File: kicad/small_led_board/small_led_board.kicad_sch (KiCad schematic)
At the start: 106 parts, among them J1 Breakout to FPGA, Q1 IRLZ44N, Q10 IRF4905, Q11 IRF4905, Q12 IRF4905, Q13 IRF4905, Q14 IRF4905, Q15 IRLZ44N, Q16 IRLZ44N, Q17 IRLZ44N, Q18 IRLZ44N, Q19 IRLZ44N, Q2 IRLZ44N, Q20 IRLZ44N, Q3 IRLZ44N, Q4 IRLZ44N, Q5 IRLZ44N, Q6 IRLZ44N, Q7 IRLZ44N, Q8 IRLZ44N, Q9 IRF4905, U1 74HC595, U2 74HC595, U3 74HC595

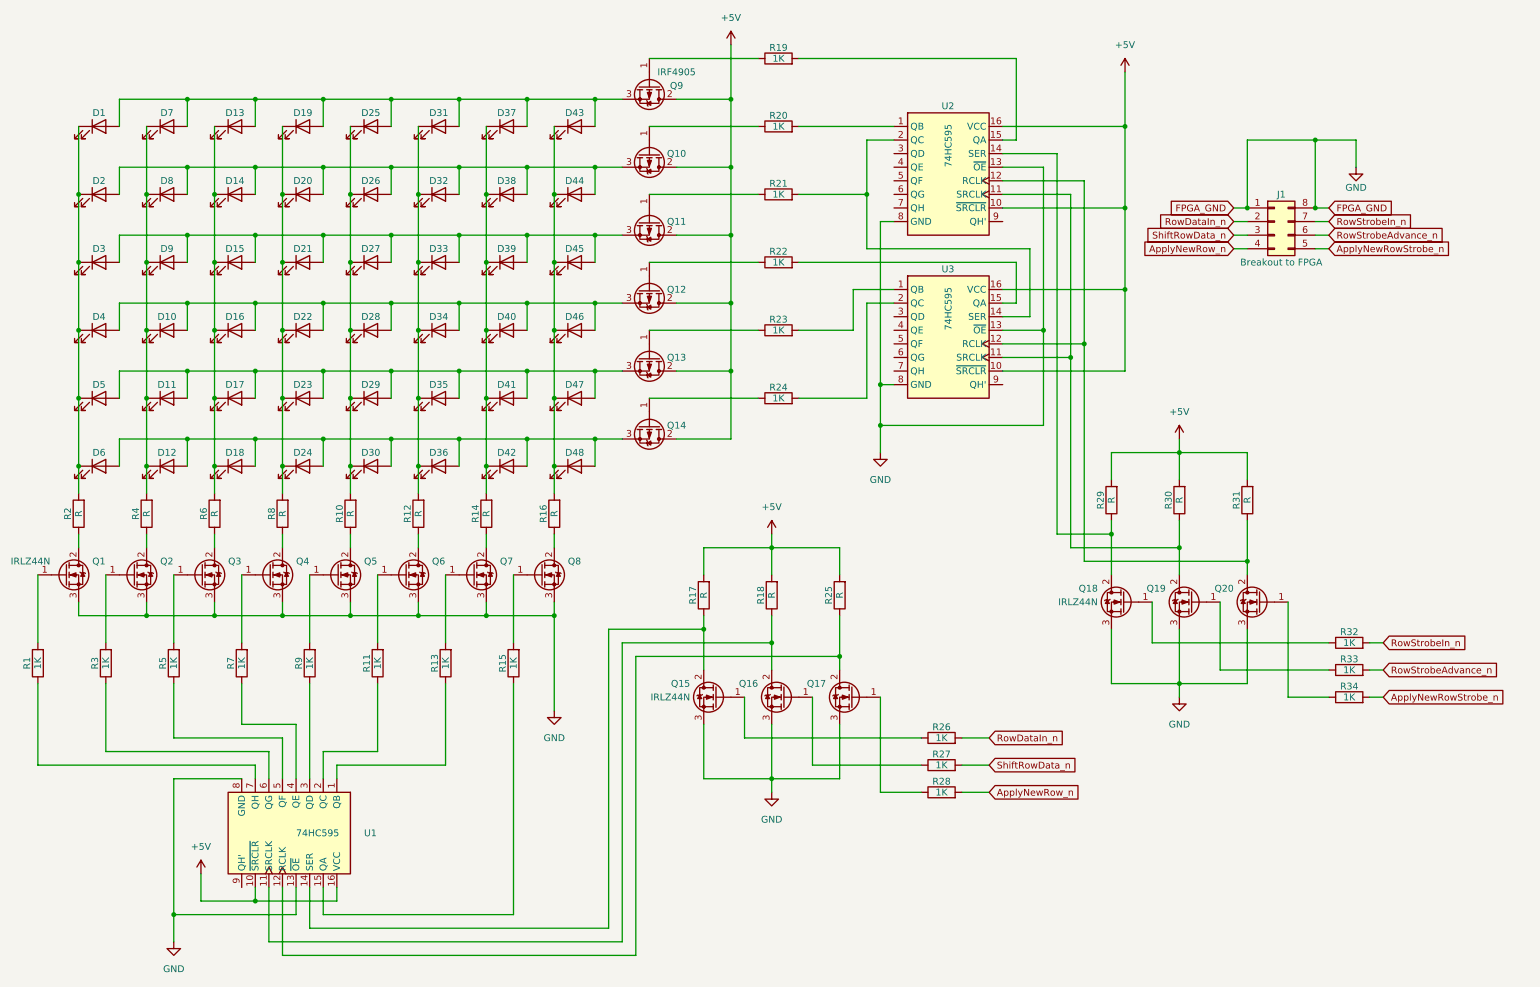
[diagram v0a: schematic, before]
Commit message: small_led_board: Schematic updated, DRC pass
- Schematic passes DRC check without any issue
- LED resistors still need to be calculated after that the schematic should be finished
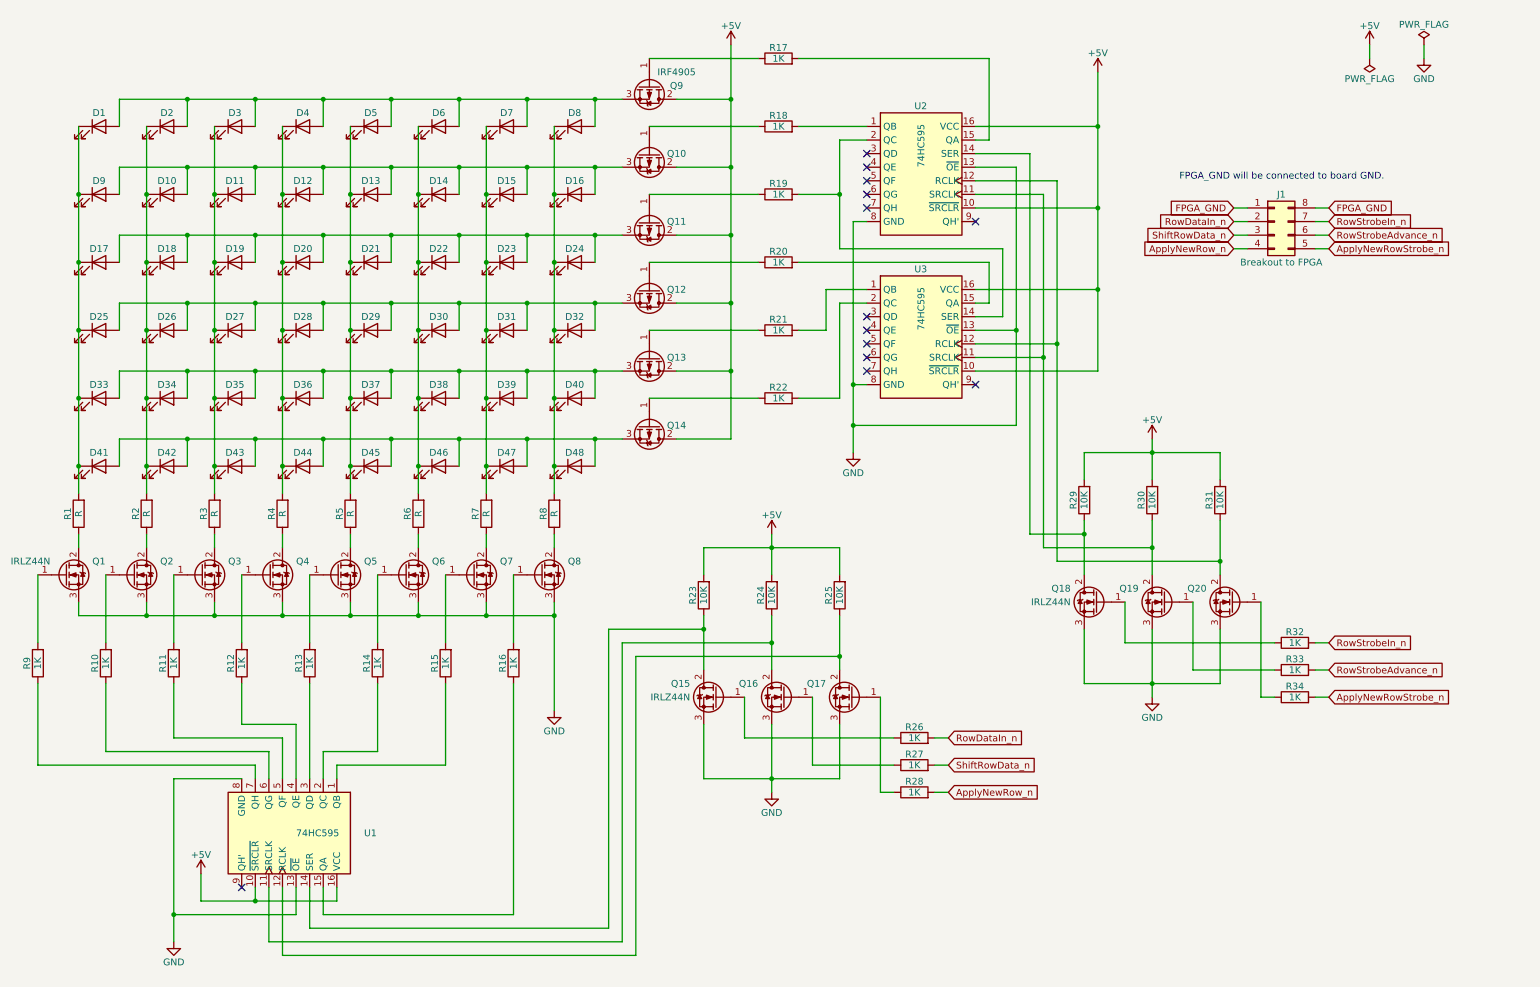
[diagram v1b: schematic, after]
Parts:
- D1, D10, D11, D12, D13, D14, D15, D16, D17, D18, D19, D2, D20, D21, D22, D23, D24, D25, D26, D27, D28, D29, D3, D30, D31, D32, D33, D34, D35, D36, D37, D38, D39, D4, D40, D41, D42, D43, D44, D45, D46, D47, D48, D5, D6, D7, D8, D9: footprint (none) -> LED_THT:LED_D5.0mm
- J1: footprint (none) -> Connector_PinHeader_2.54mm:PinHeader_2x06_P2.54mm_Horizontal
- R1, R3, R5, R7: value 1K -> R; footprint (none) -> Resistor_THT:R_Axial_DIN0207_L6.3mm_D2.5mm_P7.62mm_Horizontal
- R10, R12, R14, R16, R17, R18: value R -> 1K; footprint (none) -> Resistor_THT:R_Axial_DIN0207_L6.3mm_D2.5mm_P7.62mm_Horizontal
- R11, R13, R15, R19, R2, R20, R21, R22, R26, R27, R28, R32, R33, R34, R4, R6, R8, R9: footprint (none) -> Resistor_THT:R_Axial_DIN0207_L6.3mm_D2.5mm_P7.62mm_Horizontal
- R23, R24: value 1K -> 10K; footprint (none) -> Resistor_THT:R_Axial_DIN0207_L6.3mm_D2.5mm_P7.62mm_Horizontal
- R25, R29, R30, R31: value R -> 10K; footprint (none) -> Resistor_THT:R_Axial_DIN0207_L6.3mm_D2.5mm_P7.62mm_Horizontal
- U1, U2, U3: footprint (none) -> Package_DIP:DIP-16_W7.62mm
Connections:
- net +5V: now also R23.2, R24.2; no longer R17.2, R18.2
- net GND: no longer J1.1 (Pin_1), J1.8 (Pin_8)
- net at Q11.1 (G): now also R19.1; no longer R21.1
- net at U2.2 (QC), U3.14 (SER): now also R19.2; no longer R21.2
- net at Q5.1 (G): now also R13.2; no longer R9.2
- net at Q5.2 (D): now also R5.1; no longer R10.1
- net at Q12.1 (G): now also R20.1; no longer R22.1
- net at Q6.1 (G): now also R14.2; no longer R11.2
- net at Q6.2 (D): now also R6.1; no longer R12.1
- net at R23.1: now also Q15.2 (D), U1.14 (SER); no longer Q13.1 (G)
- net at Q10.1 (G): now also R18.1; no longer R20.1
- net at R7.2: now also D15.1 (K), D23.1 (K), D31.1 (K), D39.1 (K), D47.1 (K), D7.1 (K); no longer Q4.1 (G)
- net at R8.1: now also Q8.2 (D); no longer Q4.2 (D)
- net at Q9.1 (G): now also R17.1; no longer R19.1
- net at R1.2: now also D1.1 (K), D17.1 (K), D25.1 (K), D33.1 (K), D41.1 (K), D9.1 (K); no longer Q1.1 (G)
- net at R2.1: now also Q2.2 (D); no longer Q1.2 (D)
- net at U2.1 (QB): now also R18.2; no longer R20.2
- net at Q16.2 (D), U1.11 (SRCLK): now also R24.1; no longer R18.1
- net at U1.1 (QB): now also R15.1; no longer R13.1
- net at Q7.1 (G): now also R15.2; no longer R13.2
- net at Q3.2 (D): now also R3.1; no longer R6.1
- net at R14.1: now also U1.2 (QC); no longer Q7.2 (D)
- net at Q14.1 (G): now also R22.1; no longer R24.1
- net at U3.2 (QC): now also R22.2; no longer R24.2
- net at U3.1 (QB): now also R21.2; no longer R23.2
- net at U1.6 (QG): now also R10.1; no longer R3.1
- net at R3.2: now also D11.1 (K), D19.1 (K), D27.1 (K), D3.1 (K), D35.1 (K), D43.1 (K); no longer Q2.1 (G)
- net at R11.1: now also U1.5 (QF); no longer U1.2 (QC)
- net at U1.15 (QA): now also R16.1; no longer R15.1
- net at U1.3 (QD): now also R13.1; no longer R9.1
- net at U1.4 (QE): now also R12.1; no longer R7.1
- net at R1.1: now also Q1.2 (D); no longer U1.7 (QH)
- net at Q8.1 (G): now also R16.2; no longer R15.2
- net at R4.1: now also Q4.2 (D); no longer Q2.2 (D)
- net at R5.2: now also D13.1 (K), D21.1 (K), D29.1 (K), D37.1 (K), D45.1 (K), D5.1 (K); no longer Q3.1 (G)
- net at U3.15 (QA): now also R20.2; no longer R22.2
- net at U2.15 (QA): now also R17.2; no longer R19.2
- new net: D10.2 (A), D11.2 (A), D12.2 (A), D13.2 (A), D14.2 (A), D15.2 (A), D16.2 (A), D9.2 (A), Q10.3 (S)
- new net: D14.1 (K), D22.1 (K), D30.1 (K), D38.1 (K), D46.1 (K), D6.1 (K), R6.2
- new net: D33.2 (A), D34.2 (A), D35.2 (A), D36.2 (A), D37.2 (A), D38.2 (A), D39.2 (A), D40.2 (A), Q13.3 (S)
- new net: D1.2 (A), D2.2 (A), D3.2 (A), D4.2 (A), D5.2 (A), D6.2 (A), D7.2 (A), D8.2 (A), Q9.3 (S)
- new net: D12.1 (K), D20.1 (K), D28.1 (K), D36.1 (K), D4.1 (K), D44.1 (K), R4.2
- new net: D17.2 (A), D18.2 (A), D19.2 (A), D20.2 (A), D21.2 (A), D22.2 (A), D23.2 (A), D24.2 (A), Q11.3 (S)
- new net: D41.2 (A), D42.2 (A), D43.2 (A), D44.2 (A), D45.2 (A), D46.2 (A), D47.2 (A), D48.2 (A), Q14.3 (S)
- new net: D10.1 (K), D18.1 (K), D2.1 (K), D26.1 (K), D34.1 (K), D42.1 (K), R2.2
- new net: D25.2 (A), D26.2 (A), D27.2 (A), D28.2 (A), D29.2 (A), D30.2 (A), D31.2 (A), D32.2 (A), Q12.3 (S)
- new net: D16.1 (K), D24.1 (K), D32.1 (K), D40.1 (K), D48.1 (K), D8.1 (K), R8.2
- new net: Q4.1 (G), R12.2
- new net: Q13.1 (G), R21.1
- new net: Q1.1 (G), R9.2
- new net: Q7.2 (D), R7.1
- new net: Q3.1 (G), R11.2
- new net: R9.1, U1.7 (QH)
- new net: Q2.1 (G), R10.2
- new net FPGA_GND: J1.1 (Pin_1), J1.8 (Pin_8)
- no-connect marks 0 -> 13
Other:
- note added: "FPGA_GND will be connected to board GND."
- moved on the sheet: Q18, Q19, Q20, U2, U3

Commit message: small_led_board: Schematics done
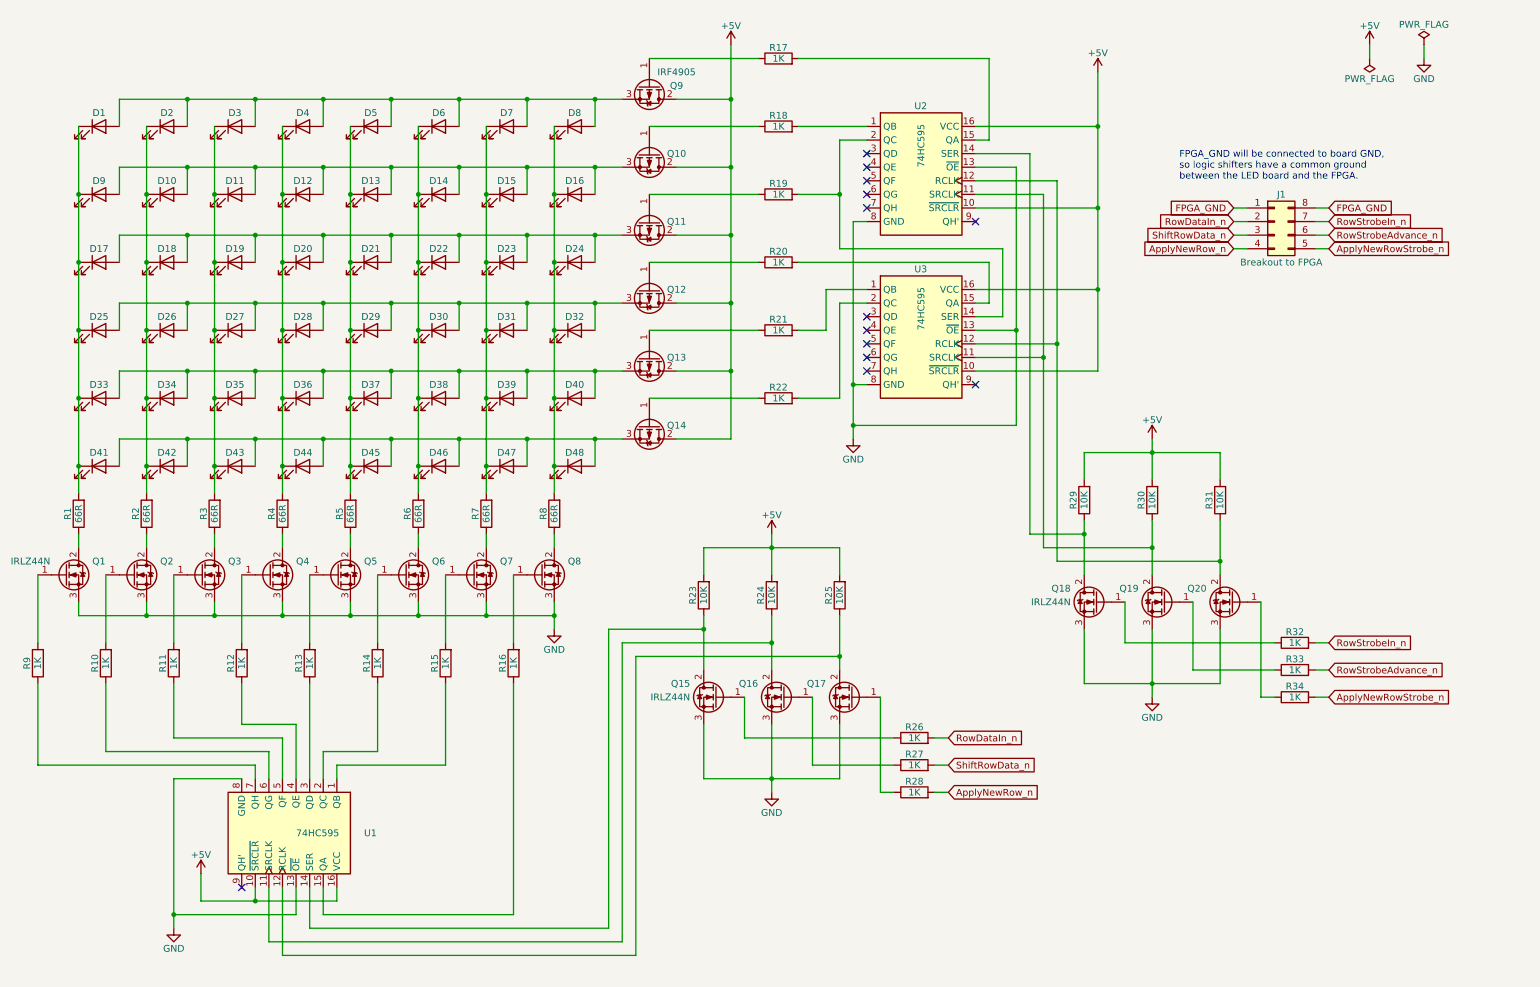
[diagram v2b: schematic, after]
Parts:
- R1, R2, R3, R4, R5, R6, R7, R8: value R -> 66R
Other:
- note added: "FPGA_GND will be connected to board GND, so logic shifters have a common ground between the LED board and the FPGA."
- note removed: "FPGA_GND will be connected to board GND."
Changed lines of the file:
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@@
     (stroke (width 0) (type default))
   )
-  (wire (pts (xy 43.18 182.88) (xy 43.18 187.96))
+  (wire (pts (xy 43.18 182.88) (xy 43.18 185.42))
     (stroke (width 0) (type default))
   )
@@
     (stroke (width 0) (type default))
   )
-  (wire (pts (xy 114.3 127) (xy 114.3 144.78))
+  (wire (pts (xy 114.3 127) (xy 114.3 129.54))
     (stroke (width 0) (type default))
   )
@@
     (stroke (width 0) (type default))
   )
-  (wire (pts (xy 170.18 91.44) (xy 170.18 96.52))
+  (wire (pts (xy 170.18 91.44) (xy 170.18 93.98))
     (stroke (width 0) (type default))
   )
@@
     (stroke (width 0) (type default))
   )
-  (text "FPGA_GND will be connected to board GND." (at 231.14 45.72 0)
+  (text "FPGA_GND will be connected to board GND,\nso logic shifters have a common ground\nbetween the LED board and the FPGA."
+    (at 231.14 45.72 0)
     (effects (font (size 1.27 1.27)) (justify left bottom))
   )
@@
     )
   )
-  (symbol (lib_id "power:GND") (at 43.18 187.96 0) (unit 1)
+  (symbol (lib_id "power:GND") (at 43.18 185.42 0) (unit 1)
     (in_bom yes) (on_board yes) (dnp no)
-    (property "Reference" "#PWR02" (at 43.18 194.31 0)
+    (property "Reference" "#PWR02" (at 43.18 191.77 0)
       (effects (font (size 1.27 1.27)) hide)
     )
-    (property "Value" "GND" (at 43.18 191.77 0)
+    (property "Value" "GND" (at 43.18 189.23 0)
       (effects (font (size 1.27 1.27)))
     )
-    (property "Footprint" "" (at 43.18 187.96 0)
+    (property "Footprint" "" (at 43.18 185.42 0)
       (effects (font (size 1.27 1.27)) hide)
     )
-    (property "Datasheet" "" (at 43.18 187.96 0)
+    (property "Datasheet" "" (at 43.18 185.42 0)
       (effects (font (size 1.27 1.27)) hide)
     )
@@
       (effects (font (size 1.27 1.27)))
     )
-    (property "Value" "R" (at 114.3 107.95 90)
+    (property "Value" "66R" (at 114.3 107.95 90)
       (effects (font (size 1.27 1.27)))
     )
@@
       (effects (font (size 1.27 1.27)))
     )
-    (property "Value" "R" (at 50.8 107.95 90)
+    (property "Value" "66R" (at 50.8 107.95 90)
       (effects (font (size 1.27 1.27)))
     )
@@
       (effects (font (size 1.27 1.27)))
     )
-    (property "Value" "R" (at 38.1 107.95 90)
+    (property "Value" "66R" (at 38.1 107.95 90)
       (effects (font (size 1.27 1.27)))
     )
@@
       (effects (font (size 1.27 1.27)))
     )
-    (property "Value" "R" (at 25.4 107.95 90)
+    (property "Value" "66R" (at 25.4 107.95 90)
       (effects (font (size 1.27 1.27)))
     )
@@
     )
   )
-  (symbol (lib_id "power:GND") (at 114.3 144.78 0) (unit 1)
+  (symbol (lib_id "power:GND") (at 114.3 129.54 0) (unit 1)
     (in_bom yes) (on_board yes) (dnp no)
-    (property "Reference" "#PWR01" (at 114.3 151.13 0)
+    (property "Reference" "#PWR01" (at 114.3 135.89 0)
       (effects (font (size 1.27 1.27)) hide)
     )
-    (property "Value" "GND" (at 114.3 148.59 0)
+    (property "Value" "GND" (at 114.3 133.35 0)
       (effects (font (size 1.27 1.27)))
     )
-    (property "Footprint" "" (at 114.3 144.78 0)
+    (property "Footprint" "" (at 114.3 129.54 0)
       (effects (font (size 1.27 1.27)) hide)
     )
-    (property "Datasheet" "" (at 114.3 144.78 0)
+    (property "Datasheet" "" (at 114.3 129.54 0)
       (effects (font (size 1.27 1.27)) hide)
     )
@@
       (effects (font (size 1.27 1.27)))
     )
-    (property "Value" "R" (at 63.5 107.95 90)
+    (property "Value" "66R" (at 63.5 107.95 90)
       (effects (font (size 1.27 1.27)))
     )
@@
       (effects (font (size 1.27 1.27)))
     )
-    (property "Value" "R" (at 101.6 107.95 90)
+    (property "Value" "66R" (at 101.6 107.95 90)
       (effects (font (size 1.27 1.27)))
     )
@@
       (effects (font (size 1.27 1.27)))
     )
-    (property "Value" "R" (at 88.9 107.95 90)
+    (property "Value" "66R" (at 88.9 107.95 90)
       (effects (font (size 1.27 1.27)))
     )
@@
     )
   )
-  (symbol (lib_id "power:GND") (at 170.18 96.52 0) (unit 1)
+  (symbol (lib_id "power:GND") (at 170.18 93.98 0) (unit 1)
     (in_bom yes) (on_board yes) (dnp no)
-    (property "Reference" "#PWR07" (at 170.18 102.87 0)
+    (property "Reference" "#PWR07" (at 170.18 100.33 0)
       (effects (font (size 1.27 1.27)) hide)
     )
-    (property "Value" "GND" (at 170.18 100.33 0)
+    (property "Value" "GND" (at 170.18 97.79 0)
       (effects (font (size 1.27 1.27)))
     )
-    (property "Footprint" "" (at 170.18 96.52 0)
+    (property "Footprint" "" (at 170.18 93.98 0)
       (effects (font (size 1.27 1.27)) hide)
     )
-    (property "Datasheet" "" (at 170.18 96.52 0)
+    (property "Datasheet" "" (at 170.18 93.98 0)
       (effects (font (size 1.27 1.27)) hide)
     )
@@
       (effects (font (size 1.27 1.27)))
     )
-    (property "Value" "R" (at 76.2 107.95 90)
+    (property "Value" "66R" (at 76.2 107.95 90)
       (effects (font (size 1.27 1.27)))
     )

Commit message: small_led_board: PCB started
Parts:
- added J2: +5V IN, Connector_BarrelJack:BarrelJack_Horizontal, symbol Connector:Barrel_Jack
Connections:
- net +5V: now also Q10.3 (S), Q11.3 (S), Q12.3 (S), Q13.3 (S), Q14.3 (S), Q9.3 (S), J2.2; no longer Q10.2 (D), Q11.2 (D), Q12.2 (D), Q13.2 (D), Q14.2 (D), Q9.2 (D)
- net GND: now also J2.1
- net at D10.2 (A), D11.2 (A), D12.2 (A)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: now also Q10.2 (D); no longer Q10.3 (S)
- net at D33.2 (A), D34.2 (A), D35.2 (A)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: now also Q13.2 (D); no longer Q13.3 (S)
- net at D1.2 (A), D2.2 (A), D3.2 (A)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: now also Q9.2 (D); no longer Q9.3 (S)
- net at D17.2 (A), D18.2 (A), D19.2 (A)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: now also Q11.2 (D); no longer Q11.3 (S)
- net at D41.2 (A), D42.2 (A), D43.2 (A)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: now also Q14.2 (D); no longer Q14.3 (S)
- net at D25.2 (A), D26.2 (A), D27.2 (A)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: now also Q12.2 (D); no longer Q12.3 (S)
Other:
- moved on the sheet: J1, Q9

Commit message: small_led_board: Placed and Routed PCB
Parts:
- removed J1: Breakout to FPGA, Connector_PinHeader_2.54mm:PinHeader_2x06_P2.54mm_Horizontal, symbol Connector_Generic:Conn_02x04_Counter_Clockwise
- removed J2: +5V IN, Connector_BarrelJack:BarrelJack_Horizontal, symbol Connector:Barrel_Jack
- added J1: TO FPGA, Connector_PinSocket_2.54mm:PinSocket_2x04_P2.54mm_Horizontal, symbol Connector_Generic:Conn_02x04_Odd_Even
- added J2: +5V IN, Connector_BarrelJack:BarrelJack_Horizontal, symbol Connector:Barrel_Jack_Switch
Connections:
- net +5V: now also J2.1
- net ApplyNewRowStrobe_n: now also J1.6 (Pin_6)
- net ApplyNewRow_n: now also J1.5 (Pin_5)
- net GND: now also J1.1 (Pin_1), J1.2 (Pin_2), J2.2, J2.3
- net RowDataIn_n: now also J1.7 (Pin_7)
- net RowStrobeAdvance_n: now also J1.8 (Pin_8)
- net RowStrobeIn_n: now also J1.4 (Pin_4)
- net ShiftRowData_n: now also J1.3 (Pin_3)
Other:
- note added: "Pin 1 and 2 refer to the FPGA GND and will be connected to board GND, so logic shifters have a common ground between the LED board and the FPGA."
- note removed: "FPGA_GND will be connected to board GND, so logic shifters have a common ground between the LED board and the FPGA."

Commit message: small_led_board: Renamed pin for more consistency
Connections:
- net RowStrobeAdvance_n renamed ShiftRowStrobe_n
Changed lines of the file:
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@@
     )
   )
-  (global_label "RowStrobeAdvance_n" (shape input) (at 259.08 76.2 0) (fields_autoplaced)
+  (global_label "ShiftRowStrobe_n" (shape input) (at 259.08 76.2 0) (fields_autoplaced)
     (effects (font (size 1.27 1.27)) (justify left))
-    (property "Intersheetrefs" "${INTERSHEET_REFS}" (at 281.7197 76.2 0)
+    (property "Intersheetrefs" "${INTERSHEET_REFS}" (at 278.454 76.2 0)
       (effects (font (size 1.27 1.27)) (justify left) hide)
     )
   )
-  (global_label "RowStrobeAdvance_n" (shape input) (at 259.08 137.16 0) (fields_autoplaced)
+  (global_label "ShiftRowStrobe_n" (shape input) (at 259.08 137.16 0) (fields_autoplaced)
     (effects (font (size 1.27 1.27)) (justify left))
-    (property "Intersheetrefs" "${INTERSHEET_REFS}" (at 281.7197 137.16 0)
+    (property "Intersheetrefs" "${INTERSHEET_REFS}" (at 278.454 137.16 0)
       (effects (font (size 1.27 1.27)) (justify left) hide)
     )
